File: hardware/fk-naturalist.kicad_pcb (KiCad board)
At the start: 2 copper layers, 28.7 x 87.4 mm, 90 parts, among them J1 MICRO-USB, J2 CONN_01X03, J3 Conn_01x08, J4 Conn_01x02, J5 Conn_01x01, J6 CONN-HDR-2x5, J8 Conn_01x01, M1 MOUNT_HOLE, M2 MOUNT_HOLE, M3 MOUNT_HOLE, M4 MOUNT_HOLE, Q1 2N7002LT1G, Q2 2N7002LT1G, Q3 2N7002LT1G, Q4 2N7002LT1G, SW1 SPNO, U1 ATSAMD21G18A-AU, U101 TSL2591, U102 MPL3115A2, U103 BNO055, U104 SHT31, U2 MCP1700T-XXX2E, U3 MAX4466, U4 S25FL1xxK0XM, Y1 FC-135, Y101 FC-135

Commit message: Just tweaking the locations of things.
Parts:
- moved J5 6.21 mm to (142.8, 120.3), turned to 270 degrees
- moved R27 4.64 mm to (140.9, 123.5), turned to 270 degrees
- moved J8 4.21 mm to (140.6, 120.3), turned to 270 degrees
- moved R26 4.17 mm to (142.6, 123.5), turned to 270 degrees
- moved R6 2.44 mm to (142.4, 130.6)
- moved R29 1.63 mm to (145.7, 130.6)
- moved R28 1.58 mm to (147.3, 130.6)
- moved R7 1.42 mm to (144.0, 130.6)
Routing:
- net /SDA: track 68.9 -> 77.1 mm, vias 4 -> 5
- net /SDA2: track 25.4 -> 17.4 mm
- net /SCL: track 75.0 -> 79.1 mm, vias 3 -> 4
- net /SDA3: track 62.2 -> 59.2 mm
- net /D13: track 36.0 -> 33.4 mm, vias 3 -> 2
- net VUSB: track 35.2 -> 33.4 mm
- net 3V3: track 273.7 -> 272.0 mm
- net /SCL3: track 61.4 -> 62.5 mm

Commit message: Adding D30 and D31 to header.
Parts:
- J3: value Conn_01x08 -> Conn_01x10; footprint Socket_Strips:Socket_Strip_Straight_1x08_Pitch2.54mm -> Socket_Strips:Socket_Strip_Straight_1x10_Pitch2.54mm
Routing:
- net /D30: track 0.00 -> 33.4 mm, vias 0 -> 1
- net /D31: track 0.00 -> 32.7 mm, vias 0 -> 1
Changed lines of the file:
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@@
 (kicad_pcb (version 4) (host pcbnew 4.0.7-e2-6376~58~ubuntu16.04.1)
   (general
-    (links 203)
+    (links 205)
     (no_connects 0)
-    (area 106.352905 47.75 165.914286 159.377948)
+    (area 125.718499 67.742999 154.578121 155.274081)
     (thickness 1.6)
     (drawings 33)
-    (tracks 818)
+    (tracks 840)
     (zones 0)
     (modules 90)
@@
     )
   )
-  (module Socket_Strips:Socket_Strip_Straight_1x08_Pitch2.54mm (layer F.Cu)
+  (module Socket_Strips:Socket_Strip_Straight_1x10_Pitch2.54mm (layer F.Cu)
     (at 152.6286 150.7998 180)
-    (descr "Through hole straight socket strip, 1x08, 2.54mm pitch, single row")
-    (tags "Through hole socket strip THT 1x08 2.54mm single row")
-    (fp_text reference J3 (at 0 -2.33 180) (layer F.SilkS) hide
+    (descr "Through hole straight socket strip, 1x10, 2.54mm pitch, single row")
+    (tags "Through hole socket strip THT 1x10 2.54mm single row")
+    (fp_text reference J3 (at 0 -2.33 180) (layer F.SilkS)
       (effects (font (size 1 1) (thickness 0.15)))
     )
-    (fp_text value Conn_01x08 (at 0 20.11 180) (layer F.Fab) hide
+    (fp_text value Conn_01x10 (at 0 25.19 180) (layer F.Fab)
       (effects (font (size 1 1) (thickness 0.15)))
     )
-    (fp_line (start -1.27 -1.27) (end -1.27 19.05) (layer F.Fab) (width 0.1))
-    (fp_line (start -1.27 19.05) (end 1.27 19.05) (layer F.Fab) (width 0.1))
-    (fp_line (start 1.27 19.05) (end 1.27 -1.27) (layer F.Fab) (width 0.1))
+    (fp_line (start -1.27 -1.27) (end -1.27 24.13) (layer F.Fab) (width 0.1))
+    (fp_line (start -1.27 24.13) (end 1.27 24.13) (layer F.Fab) (width 0.1))
+    (fp_line (start 1.27 24.13) (end 1.27 -1.27) (layer F.Fab) (width 0.1))
     (fp_line (start 1.27 -1.27) (end -1.27 -1.27) (layer F.Fab) (width 0.1))
-    (fp_line (start -1.33 1.27) (end -1.33 19.11) (layer F.SilkS) (width 0.12))
-    (fp_line (start -1.33 19.11) (end 1.33 19.11) (layer F.SilkS) (width 0.12))
-    (fp_line (start 1.33 19.11) (end 1.33 1.27) (layer F.SilkS) (width 0.12))
+    (fp_line (start -1.33 1.27) (end -1.33 24.19) (layer F.SilkS) (width 0.12))
+    (fp_line (start -1.33 24.19) (end 1.33 24.19) (layer F.SilkS) (width 0.12))
+    (fp_line (start 1.33 24.19) (end 1.33 1.27) (layer F.SilkS) (width 0.12))
     (fp_line (start 1.33 1.27) (end -1.33 1.27) (layer F.SilkS) (width 0.12))
     (fp_line (start -1.33 0) (end -1.33 -1.33) (layer F.SilkS) (width 0.12))
     (fp_line (start -1.33 -1.33) (end 0 -1.33) (layer F.SilkS) (width 0.12))
-    (fp_line (start -1.8 -1.8) (end -1.8 19.55) (layer F.CrtYd) (width 0.05))
-    (fp_line (start -1.8 19.55) (end 1.8 19.55) (layer F.CrtYd) (width 0.05))
-    (fp_line (start 1.8 19.55) (end 1.8 -1.8) (layer F.CrtYd) (width 0.05))
+    (fp_line (start -1.8 -1.8) (end -1.8 24.65) (layer F.CrtYd) (width 0.05))
+    (fp_line (start -1.8 24.65) (end 1.8 24.65) (layer F.CrtYd) (width 0.05))
+    (fp_line (start 1.8 24.65) (end 1.8 -1.8) (layer F.CrtYd) (width 0.05))
     (fp_line (start 1.8 -1.8) (end -1.8 -1.8) (layer F.CrtYd) (width 0.05))
-    (fp_text user %R (at 0 -2.33 180) (layer F.Fab) hide
+    (fp_text user %R (at 0 -2.33 180) (layer F.Fab)
       (effects (font (size 1 1) (thickness 0.15)))
     )
@@
     (pad 8 thru_hole oval (at 0 17.78 180) (size 1.7 1.7) (drill 1) (layers *.Cu *.Mask)
       (net 1 GND))
-    (model ${KISYS3DMOD}/Socket_Strips.3dshapes/Socket_Strip_Straight_1x08_Pitch2.54mm.wrl
-      (at (xyz 0 -0.35 0))
+    (pad 9 thru_hole oval (at 0 20.32 180) (size 1.7 1.7) (drill 1) (layers *.Cu *.Mask)
+      (net 43 /D30))
+    (pad 10 thru_hole oval (at 0 22.86 180) (size 1.7 1.7) (drill 1) (layers *.Cu *.Mask)
+      (net 44 /D31))
+    (model ${KISYS3DMOD}/Socket_Strips.3dshapes/Socket_Strip_Straight_1x10_Pitch2.54mm.wrl
+      (at (xyz 0 -0.45 0))
       (scale (xyz 1 1 1))
       (rotate (xyz 0 0 270))
@@
   (segment (start 145.084187 109.081314) (end 145.084187 110.371093) (width 0.254) (layer F.Cu) (net 42))
   (via (at 145.084187 110.371093) (size 0.5) (drill 0.3) (layers F.Cu B.Cu) (net 42))
+  (segment (start 153.010393 114.065693) (end 146.1008 107.1561) (width 0.254) (layer B.Cu) (net 43))
+  (segment (start 145.94839 103.93679) (end 145.94839 107.00369) (width 0.254) (layer B.Cu) (net 43))
+  (segment (start 145.94839 107.00369) (end 146.1008 107.1561) (width 0.254) (layer B.Cu) (net 43))
+  (segment (start 145.5928 103.5812) (end 145.94839 103.93679) (width 0.254) (layer B.Cu) (net 43))
+  (segment (start 144.720458 105.040629) (end 145.5928 104.168287) (width 0.254) (layer F.Cu) (net 43))
+  (segment (start 145.5928 104.168287) (end 145.5928 103.5812) (width 0.254) (layer F.Cu) (net 43))
+  (via (at 145.5928 103.5812) (size 0.5) (drill 0.3) (layers F.Cu B.Cu) (net 43))
+  (segment (start 153.010393 115.789712) (end 153.010393 114.065693) (width 0.254) (layer B.Cu) (net 43))
+  (segment (start 150.82525 128.67645) (end 150.82525 127.3207) (width 0.254) (layer B.Cu) (net 43))
+  (segment (start 150.82525 127.3207) (end 153.010394 125.135556) (width 0.254) (layer B.Cu) (net 43))
+  (segment (start 153.010394 125.135556) (end 153.010393 115.789712) (width 0.254) (layer B.Cu) (net 43))
+  (segment (start 152.6286 130.4798) (end 150.82525 128.67645) (width 0.254) (layer B.Cu) (net 43))
+  (segment (start 146.3548 102.108) (end 146.104801 102.357999) (width 0.254) (layer F.Cu) (net 44))
+  (segment (start 145.856518 102.357999) (end 144.897234 103.317283) (width 0.254) (layer F.Cu) (net 44))
+  (segment (start 146.104801 102.357999) (end 145.856518 102.357999) (width 0.254) (layer F.Cu) (net 44))
+  (segment (start 144.897234 103.317283) (end 144.897234 104.156747) (width 0.254) (layer F.Cu) (net 44))
+  (segment (start 144.897234 104.156747) (end 144.366905 104.687076) (width 0.254) (layer F.Cu) (net 44))
+  (segment (start 146.3548 102.108) (end 146.3548 106.7308) (width 0.254) (layer B.Cu) (net 44))
+  (segment (start 153.478599 127.089801) (end 152.6286 127.9398) (width 0.254) (layer B.Cu) (net 44))
+  (segment (start 146.3548 106.7308) (end 153.478599 113.854599) (width 0.254) (layer B.Cu) (net 44))
+  (segment (start 153.478599 113.854599) (end 153.478599 127.089801) (width 0.254) (layer B.Cu) (net 44))
+  (via (at 146.3548 102.108) (size 0.5) (drill 0.3) (layers F.Cu B.Cu) (net 44))
   (segment (start 143.7005 106.045) (end 144.8816 106.045) (width 0.254) (layer F.Cu) (net 46))
   (segment (start 146.1008 103.7862) (end 146.1008 104.8258) (width 0.254) (layer F.Cu) (net 46))
@@
     (connect_pads (clearance 0.2032))
     (min_thickness 0.253)
-    (fill (arc_segments 32) (thermal_gap 0.254) (thermal_bridge_width 0.254) (smoothing chamfer))
+    (fill yes (arc_segments 32) (thermal_gap 0.254) (thermal_bridge_width 0.254) (smoothing chamfer))
     (polygon
       (pts
@@
     (connect_pads (clearance 0.2032))
     (min_thickness 0.253)
-    (fill (arc_segments 32) (thermal_gap 0.254) (thermal_bridge_width 0.254) (smoothing chamfer))
+    (fill yes (arc_segments 32) (thermal_gap 0.254) (thermal_bridge_width 0.254) (smoothing chamfer))
     (polygon
       (pts
@@
     (connect_pads (clearance 0.2032))
     (min_thickness 0.253)
-    (fill (arc_segments 32) (thermal_gap 0.254) (thermal_bridge_width 0.254) (smoothing chamfer))
+    (fill yes (arc_segments 32) (thermal_gap 0.254) (thermal_bridge_width 0.254) (smoothing chamfer))
     (polygon
       (pts
@@
     (connect_pads (clearance 0.2032))
     (min_thickness 0.253)
-    (fill (arc_segments 32) (thermal_gap 0.254) (thermal_bridge_width 0.254) (smoothing chamfer))
+    (fill yes (arc_segments 32) (thermal_gap 0.254) (thermal_bridge_width 0.254) (smoothing chamfer))
     (polygon
       (pts

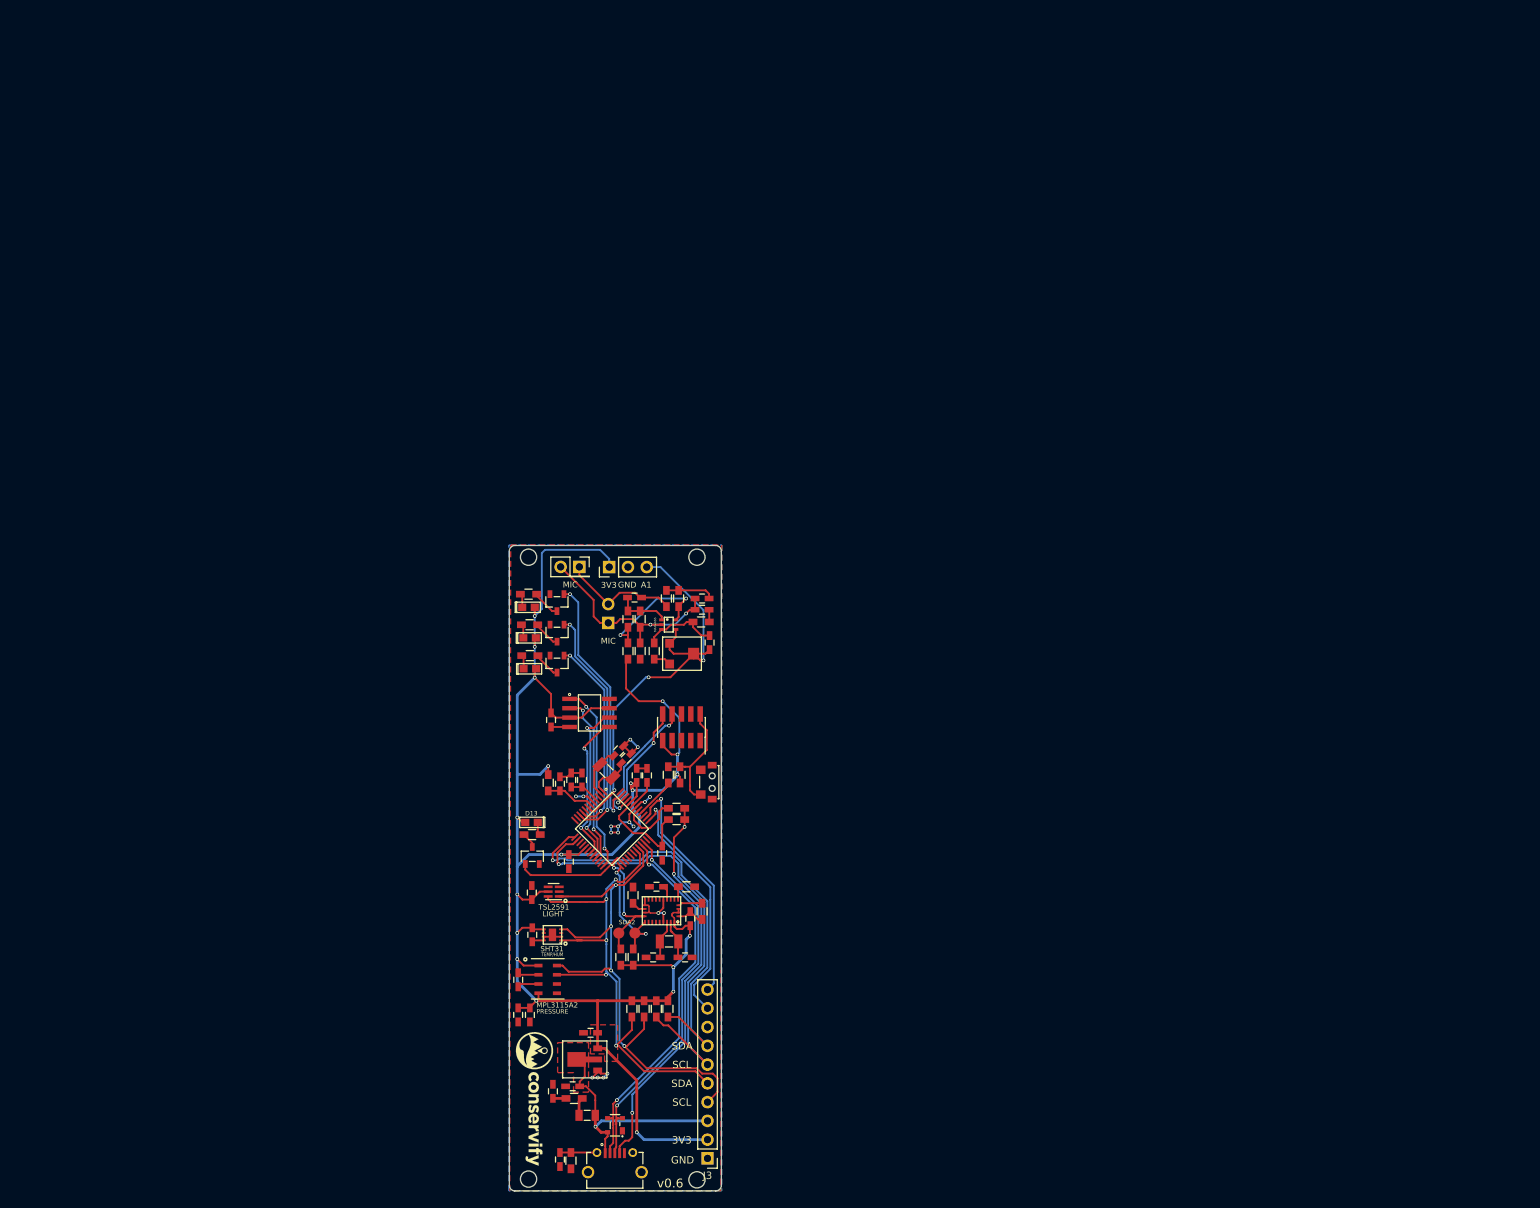
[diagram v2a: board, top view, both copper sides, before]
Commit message: Starting on the combined coreless board. Schematic is... done hopefully.
This includes the change to the new I2S chip.
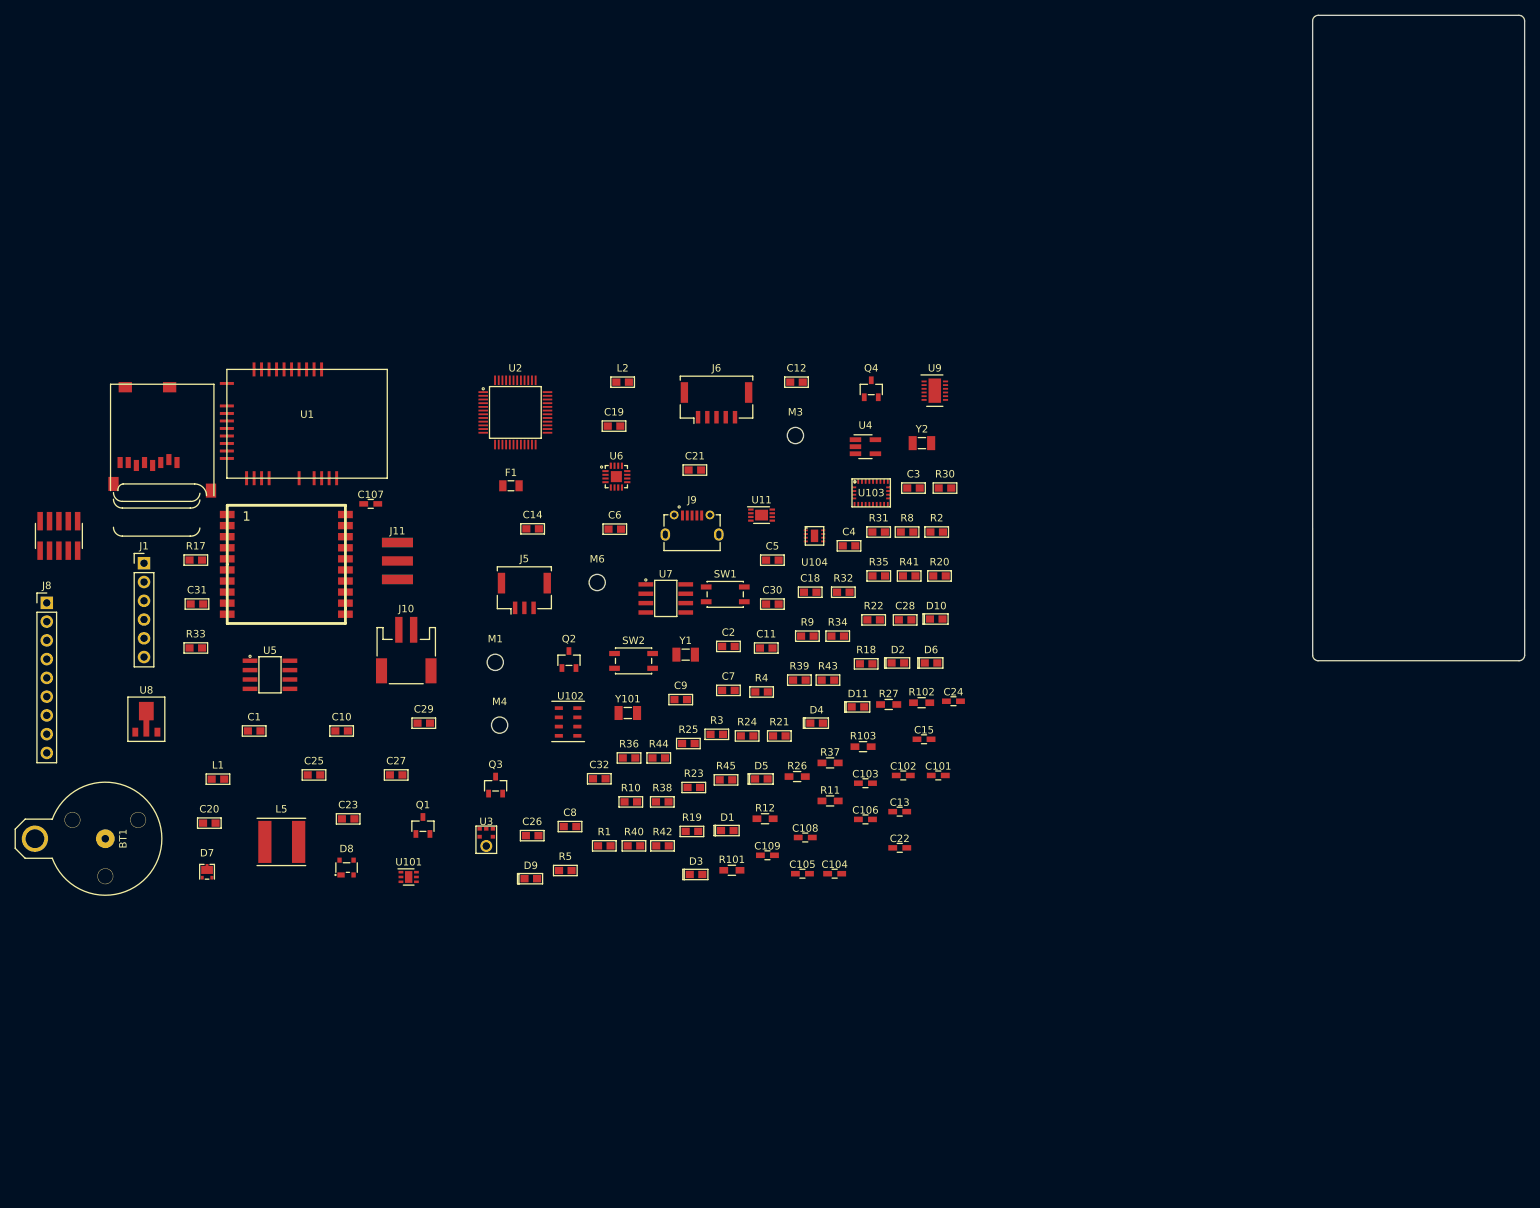
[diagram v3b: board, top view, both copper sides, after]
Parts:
- removed C16: 10uF, Capacitors_SMD:C_0603_HandSoldering
- removed C17: 100pF, Capacitors_SMD:C_0603_HandSoldering
- removed G***: LOGO, conservify:conservify_text_negative_4000
- removed J2: CONN_01X03, Socket_Strips:Socket_Strip_Straight_1x03_Pitch2.54mm
- removed J3: Conn_01x10, Socket_Strips:Socket_Strip_Straight_1x10_Pitch2.54mm
- removed J4: Conn_01x02, Socket_Strips:Socket_Strip_Straight_2x01_Pitch2.54mm
- removed L3, L4: WE-CBF, Resistors_SMD:R_0603_HandSoldering
- removed M2: MOUNT_HOLE, RocketScreamKicadLibrary:HOLE_NPTH_2.2MM
- removed MK1: CMA-4544PF-W, Socket_Strips:Socket_Strip_Straight_1x02_Pitch2.54mm
- removed R13: 1k, Resistors_SMD:R_0603_HandSoldering
- removed R14, R15: 1M, Resistors_SMD:R_0603_HandSoldering
- removed R16: 22k, Resistors_SMD:R_0603_HandSoldering
- removed R28, R29, R6, R7: 4.7K, Resistors_SMD:R_0603_HandSoldering
- removed RV1: TC33X-2-104E (100K), conservify:BOURNS-TC33X-2
- added BT1: Battery_Cell, Connectors:CR1220, F.Cu at (61.6, 107.5)
- added C19: 4.7uF 10V X5R, RocketScreamKicadLibrary:CAP-0603, F.Cu at (140.0, 51.7)
- added C20: 4.7uF 10V X5R, RocketScreamKicadLibrary:CAP-0603, F.Cu at (85.2, 105.4)
- added C21: 1uF 10V X5R, RocketScreamKicadLibrary:CAP-0603, F.Cu at (150.9, 57.6)
- added C22: 10uF, Capacitors_SMD:C_0603_HandSoldering, F.Cu at (178.7, 108.8)
- added C23: 1uF 10V X5R, RocketScreamKicadLibrary:CAP-0603, F.Cu at (104.0, 104.8)
- added C24: 10uF, Capacitors_SMD:C_0603_HandSoldering, F.Cu at (185.9, 88.9)
- added C25: 4.7uF 10V X5R, RocketScreamKicadLibrary:CAP-0603, F.Cu at (99.3, 98.9)
- added C26: 100nF, RocketScreamKicadLibrary:CAP-0603, F.Cu at (128.9, 107.1)
- added C27: 1uF 10V X5R, RocketScreamKicadLibrary:CAP-0603, F.Cu at (110.5, 98.9)
- added C28: 10nF, RocketScreamKicadLibrary:CAP-0603, F.Cu at (179.4, 77.9)
- added C29: 1uF 10V X5R, RocketScreamKicadLibrary:CAP-0603, F.Cu at (114.2, 91.9)
- added C30: 100pF, RocketScreamKicadLibrary:CAP-0603, F.Cu at (161.4, 75.8)
- added C31: 10uF, RocketScreamKicadLibrary:CAP-0603, F.Cu at (83.5, 75.7)
- added C32: 10uF, RocketScreamKicadLibrary:CAP-0603, F.Cu at (138.0, 99.4)
- added D10: Red, RocketScreamKicadLibrary:LED-0603, F.Cu at (183.6, 77.8)
- added D11: Red, RocketScreamKicadLibrary:LED-0603, F.Cu at (173.0, 89.7)
- added D6: Blue, RocketScreamKicadLibrary:LED-0603, F.Cu at (182.9, 83.7)
- added D7: PMEG3020CPA, RocketScreamKicadLibrary:SOT-1016, F.Cu at (84.9, 112.0)
- added D8: PRTR5V0U2X, RocketScreamKicadLibrary:SOT-143B, F.Cu at (103.8, 111.4)
- added D9: Green, RocketScreamKicadLibrary:LED-0603, F.Cu at (128.7, 112.9)
- added J10: S2B-PH-SM4-TB, RocketScreamKicadLibrary:S2B-PH-SM4-TB, F.Cu at (111.8, 82.0)
- added J11: RF-SMA-EDGE, RocketScreamKicadLibrary:RF-SMA-EDGE, F.Cu at (110.7, 69.9)
- added J7: CONN-HDR-2x5, conservify:HDR_2x5_Pitch1.27mm_SMD_JTAG_SWD, F.Cu at (64.8, 66.5)
- added J9: MICRO-USB, RocketScreamKicadLibrary:MICRO-USB, F.Cu at (150.5, 65.2)
- added L5: 22uH, conservify:WURTH_L_6.0x6.0, F.Cu at (94.9, 108.0)
- added M6: MOUNT_HOLE, RocketScreamKicadLibrary:HOLE_NPTH_2.2MM, F.Cu at (137.7, 72.8)
- added M7: MICROSD, conservify:MICROSD, F.Cu at (71.8, 45.9)
- added R18: 2K2, RocketScreamKicadLibrary:RES-0603, F.Cu at (174.1, 83.8)
- added R19: 2K2, RocketScreamKicadLibrary:RES-0603, F.Cu at (150.5, 106.5)
- added R20: 2K2, RocketScreamKicadLibrary:RES-0603, F.Cu at (184.0, 71.9)
- added R21: 1K18, RocketScreamKicadLibrary:RES-0603, F.Cu at (162.4, 93.6)
- added R22: 46K4, RocketScreamKicadLibrary:RES-0603, F.Cu at (175.1, 77.9)
- added R23: 100K, RocketScreamKicadLibrary:RES-0603, F.Cu at (150.8, 100.6)
- added R24: 2K94, RocketScreamKicadLibrary:RES-0603, F.Cu at (158.0, 93.6)
- added R25: 2K2, RocketScreamKicadLibrary:RES-0603, F.Cu at (150.0, 94.6)
- added R30: 330R, RocketScreamKicadLibrary:RES-0603, F.Cu at (184.8, 60.0)
- added R31: 1M, RocketScreamKicadLibrary:RES-0603, F.Cu at (175.8, 66.0)
- added R32: 10K, RocketScreamKicadLibrary:RES-0603, F.Cu at (171.0, 74.1)
- added R33: 2K2, RocketScreamKicadLibrary:RES-0603, F.Cu at (83.3, 81.7)
- added R34: 10K, RocketScreamKicadLibrary:RES-0603, F.Cu at (170.3, 80.1)
- added R35: 4.7K, RocketScreamKicadLibrary:RES-0603, F.Cu at (175.8, 71.9)
- added R36: 4.7K, RocketScreamKicadLibrary:RES-0603, F.Cu at (142.0, 96.6)
- added R37: 1k, Resistors_SMD:R_0603_HandSoldering, F.Cu at (169.2, 97.3)
- added R38: 100k, RocketScreamKicadLibrary:RES-0603, F.Cu at (146.5, 102.5)
- added R39: 1k, RocketScreamKicadLibrary:RES-0603, F.Cu at (165.1, 86.0)
- added R40: 1k, RocketScreamKicadLibrary:RES-0603, F.Cu at (142.7, 108.5)
- added R41: 180R, RocketScreamKicadLibrary:RES-0603, F.Cu at (179.9, 71.9)
- added R42: 4.7K, RocketScreamKicadLibrary:RES-0603, F.Cu at (146.5, 108.5)
- added R43: 4.7K, RocketScreamKicadLibrary:RES-0603, F.Cu at (168.9, 86.0)
- added R44: 100k, RocketScreamKicadLibrary:RES-0603, F.Cu at (146.0, 96.6)
- added R45: 22K1, RocketScreamKicadLibrary:RES-0603, F.Cu at (155.1, 99.6)
- added SW2: SPNO, conservify:SW_SPST_WURTH_1, F.Cu at (142.6, 83.4)
- added U10: FGPMMOPA6H, conservify:FGPMMOPA6H, F.Cu at (95.6, 70.4)
- added U11: MAX1704XX, Housings_DFN_QFN:DFN-8-1EP_3x2mm_Pitch0.5mm, F.Cu at (159.9, 63.7)
- added U5: S25FL116K0XMFI041, RocketScreamKicadLibrary:SOIC-8-N, F.Cu at (93.4, 85.3)
- added U6: BQ24074RGTT, RocketScreamKicadLibrary:QFN-16_3x3mm, F.Cu at (140.3, 58.5)
- added U7: PCF8523, RocketScreamKicadLibrary:SOIC-8-N, F.Cu at (147.0, 75.0)
- added U8: MCP1700T-3302E/MB, RocketScreamKicadLibrary:SOT-89, F.Cu at (76.7, 91.3)
- added U9: ISL8541x, Housings_DFN_QFN:DFN-12-1EP_3x4mm_Pitch0.5mm, F.Cu at (183.4, 46.9)
- added Y2: FC-135, RocketScreamKicadLibrary:ABS07, F.Cu at (181.7, 54.0)
- C1: value 18pF -> 4.7uF 10V X5R; footprint Capacitors_SMD:C_0603_HandSoldering -> RocketScreamKicadLibrary:CAP-0603
- C10: value 4.7nF -> 4.7uF 10V X5R; footprint Capacitors_SMD:C_0603_HandSoldering -> RocketScreamKicadLibrary:CAP-0603
- C11: value 1uF -> 100nF; footprint Capacitors_SMD:C_0603_HandSoldering -> RocketScreamKicadLibrary:CAP-0603
- C12: value 1uF -> 1uF 50V X5R; footprint Capacitors_SMD:C_0603_HandSoldering -> RocketScreamKicadLibrary:CAP-0603
- C13: value 0.1uF -> 1uF
- C14: value 4.7uF 10V X5R -> 4.7nF 25V X7R; footprint Capacitors_SMD:C_0603_HandSoldering -> RocketScreamKicadLibrary:CAP-0603
- C15: value 0.01uF -> 220pF
- C18, C7, C8: footprint Capacitors_SMD:C_0603_HandSoldering -> RocketScreamKicadLibrary:CAP-0603
- C2: value 18pF -> 100nF; footprint Capacitors_SMD:C_0603_HandSoldering -> RocketScreamKicadLibrary:CAP-0603
- C3, C4: value 100nF -> 18pF; footprint Capacitors_SMD:C_0603_HandSoldering -> RocketScreamKicadLibrary:CAP-0603
- C5: value 1uF 10V X5R -> 100nF; footprint Capacitors_SMD:C_0603_HandSoldering -> RocketScreamKicadLibrary:CAP-0603
- C6: value 100nF -> 1uF 10V X5R; footprint Capacitors_SMD:C_0603_HandSoldering -> RocketScreamKicadLibrary:CAP-0603
- C9: value 4.7uF -> 100nF; footprint Capacitors_SMD:C_0603_HandSoldering -> RocketScreamKicadLibrary:CAP-0603
- D2: value Yellow -> Green
- D3: value Blue -> Yellow
- D4: value PRTR5V0U2X -> Orange; footprint RocketScreamKicadLibrary:SOT-143B -> RocketScreamKicadLibrary:LED-0603
- D5: value Orange -> Yellow
- J1: value MICRO-USB -> CONN_01X06; footprint conservify:MICRO-USB -> Socket_Strips:Socket_Strip_Straight_1x06_Pitch2.54mm
- J5: value Conn_01x01 -> Conn_01x03; footprint Measurement_Points:Measurement_Point_Round-SMD-Pad_Small -> conservify:Molex_CLIK-Mate_502382-0370_1x03_P1.25mm_Vertical
- J6: value CONN-HDR-2x5 -> Conn_01x05; footprint Socket_Strips:Socket_Strip_Straight_2x05_Pitch1.27mm_SMD -> conservify:Molex_CLIK-Mate_502382-0570_1x05_P1.25mm_Vertical
- J8: value Conn_01x01 -> Conn_01x09; footprint Measurement_Points:Measurement_Point_Round-SMD-Pad_Small -> Socket_Strips:Socket_Strip_Straight_1x09_Pitch2.54mm
- L1, L2: footprint Inductors_SMD:L_0603_HandSoldering -> RocketScreamKicadLibrary:IND-0603
- R1: value 2k2 -> 100k; footprint Resistors_SMD:R_0603_HandSoldering -> RocketScreamKicadLibrary:RES-0603
- R10: value 1M -> 330R; footprint Resistors_SMD:R_0603_HandSoldering -> RocketScreamKicadLibrary:RES-0603
- R11: value 1k -> 10K
- R12: value 1k -> 68R
- R17: value 2k2 -> 10K; footprint Resistors_SMD:R_0603_HandSoldering -> RocketScreamKicadLibrary:RES-0603
- R2: value 330R -> 100k; footprint Resistors_SMD:R_0603_HandSoldering -> RocketScreamKicadLibrary:RES-0603
- R3: value 2k2 -> 2K2; footprint Resistors_SMD:R_0603_HandSoldering -> RocketScreamKicadLibrary:RES-0603
- R4: value 10K -> 1k; footprint Resistors_SMD:R_0603_HandSoldering -> RocketScreamKicadLibrary:RES-0603
- R5: value 2k2 -> 1k; footprint Resistors_SMD:R_0603_HandSoldering -> RocketScreamKicadLibrary:RES-0603
- R8: value 100k -> 10K; footprint Resistors_SMD:R_0603_HandSoldering -> RocketScreamKicadLibrary:RES-0603
- R9: footprint Resistors_SMD:R_0603_HandSoldering -> RocketScreamKicadLibrary:RES-0603
- SW1: footprint RocketScreamKicadLibrary:TS-018 -> conservify:SW_SPST_WURTH_1
- U1: value ATSAMD21G18A-AU -> ATWINC1500-MR210PA; footprint RocketScreamKicadLibrary:TQFP-48_7x7mm_Pitch0.5mm -> conservify:ATMEL_ATWINC1500-MR210PA
- U2: value MCP1700T-XXX2E -> ATSAMD21G18A-AU; footprint RocketScreamKicadLibrary:SOT-89 -> RocketScreamKicadLibrary:TQFP-48_7x7mm_Pitch0.5mm
- U3: value MAX4466 -> SPH0645; footprint conservify:SC70-5 -> conservify:SPH0645LM4H-B
- U4: value S25FL1xxK0XM -> 24AA02E64; footprint RocketScreamKicadLibrary:SOIC-8-N -> TO_SOT_Packages_SMD:SOT-23-5_HandSoldering
- moved J1 103.3 mm to (76.3, 70.2)
- moved C12 92.4 mm to (164.7, 45.7), turned to 0 degrees
- moved J8 89.4 mm to (63.2, 75.6), turned to 0 degrees
- moved U2 88.1 mm to (126.6, 49.8), turned to 0 degrees
- moved F1 85.9 mm to (126.0, 59.7)
- moved Q4 78.1 mm to (174.8, 46.6)
- moved C107 72.3 mm to (107.0, 62.2), turned to 0 degrees
- moved M1 70.1 mm to (123.9, 83.6)
- moved U1 68.6 mm to (98.4, 51.3), turned to 0 degrees
- moved C10 65.1 mm to (103.1, 92.9), turned to 0 degrees
- moved C11 64.9 mm to (160.6, 81.7), turned to 0 degrees
- moved L1 64.8 mm to (86.3, 99.5)
- moved U104 64.6 mm to (167.1, 66.5), turned to 0 degrees
- moved U103 63.3 mm to (174.8, 60.7), turned to 0 degrees
- moved D4 60.9 mm to (167.4, 91.9), turned to 0 degrees
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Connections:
- net /A0 renamed Net-(U1-Pad3)
- C1 pad 1: GND -> AREF
- C1 pad 2: Net-(C1-Pad2) -> GND
- C10 pad 1: Net-(C10-Pad1) -> 5V0
- C11 pad 1: VUSB -> 3V3
- C12 pad 1: 3V3 -> GND
- C12 pad 2: GND -> VEXT
- C13 pad 1: Net-(C13-Pad1) -> 3V3
- C13 pad 2: /AGND -> GND
- C14 pad 1: AREF -> Net-(C14-Pad1)
- C15 pad 1: Net-(C15-Pad1) -> 3V3
- C15 pad 2: Net-(C15-Pad2) -> GND
- C2 pad 1: GND -> AREF
- C2 pad 2: Net-(C2-Pad2) -> GND
- C3 pad 1: 3V3 -> GND
- C3 pad 2: GND -> Net-(C3-Pad2)
- C4 pad 1: Net-(C4-Pad1) -> GND
- C4 pad 2: GND -> Net-(C4-Pad2)
- C5 pad 1: Net-(C5-Pad1) -> 3V3
- C6 pad 1: AREF -> Net-(C6-Pad1)
- C7 pad 1: 3V3 -> Net-(C7-Pad1)
- C9 pad 1: 5V0 -> 3V3
- D4 pad 1: GND -> Net-(D4-Pad1)
- D4 pad 2: /USB+ -> 3V3
- J1 pad 1: VUSB -> VBAT
- J1 pad 2: /USB- -> GND
- J1 pad 3: /USB+ -> VIN
- J1 pad 4: Net-(J1-Pad4) -> 5V0
- J1 pad 5: GND -> VBUS
- J1 pad 6: Net-(C10-Pad1) -> 3V3
- J5 pad 1: /SDA2 -> GND
- J6 pad 1: GND -> 3V3
- J6 pad 2: /RST -> GND
- J6 pad 3: Net-(J6-Pad3) -> GND
- J6 pad 4: Net-(J6-Pad4) -> /SCL
- J6 pad 5: GND -> /SDA
- J8 pad 1: /D13 -> /RADIO_RST
- L1 pad 1: 5V0 -> Net-(C7-Pad1)
- L1 pad 2: Net-(F1-Pad1) -> 3V3
- L2 pad 1: Net-(C4-Pad1) -> 5V0
- L2 pad 2: 3V3 -> Net-(F1-Pad1)
- Q1 pad 1: /A3 -> /D13
- Q2 pad 1: /A4 -> /A3
- Q3 pad 1: /A5 -> /A4
- Q4 pad 1: /D13 -> /A5
- R1 pad 1: Net-(D1-Pad1) -> /WIFI_RST
- R1 pad 2: Net-(Q1-Pad3) -> GND
- R10 pad 1: Net-(C10-Pad1) -> /USER_SW
- R10 pad 2: GND -> Net-(R10-Pad2)
- R11 pad 1: /AVCC -> GND
- R11 pad 2: Net-(C13-Pad1) -> Net-(R11-Pad2)
- R12 pad 1: Net-(C13-Pad1) -> Net-(R12-Pad1)
- R12 pad 2: Net-(C15-Pad2) -> /I2S_DATA
- R17 pad 1: Net-(D5-Pad1) -> 3V3
- R17 pad 2: Net-(Q4-Pad3) -> Net-(R10-Pad2)
- R2 pad 1: /RESET -> /WIFI_EN
- R2 pad 2: /RST -> GND
- R27 pad 1: /D13 -> /SCL2
- R3 pad 1: Net-(D2-Pad1) -> Net-(D1-Pad1)
- R3 pad 2: Net-(Q2-Pad3) -> Net-(Q1-Pad3)
- R4 pad 1: 3V3 -> Net-(R4-Pad1)
- R4 pad 2: /RST -> Net-(D2-Pad1)
- R5 pad 1: Net-(D3-Pad1) -> Net-(R5-Pad1)
- R5 pad 2: Net-(Q3-Pad3) -> Net-(D3-Pad1)
- R8 pad 2: Net-(J1-Pad4) -> /RST
- R9 pad 1: Net-(J1-Pad4) -> /RESET
- R9 pad 2: /USB_ID -> /RST
- U1 pad 1: Net-(C2-Pad2) -> Net-(U1-Pad1)
- U1 pad 10: /A4 -> 3V3
- U1 pad 11: /D8 -> /WIFI_WAKE
- U1 pad 12: /D9 -> GND
- U1 pad 13: /SDA3 -> /WIFI_IRQ
- U1 pad 14: /SCL3 -> Net-(U1-Pad14)
- U1 pad 15: /D1 -> /MOSI
- U1 pad 16: /D0 -> /WIFI_CS
- U1 pad 17: 3V3 -> /MISO
- U1 pad 18: GND -> /SCK
- U1 pad 19: /MOSI -> Net-(U1-Pad19)
- U1 pad 2: Net-(C1-Pad2) -> Net-(U1-Pad2)
- U1 pad 20: /SCK -> 3V3
- U1 pad 21: /MISO -> Net-(U1-Pad21)
- U1 pad 22: /ATN -> /WIFI_EN
- U1 pad 23: /D2 -> 3V3
- U1 pad 24: /D5 -> Net-(U1-Pad24)
- U1 pad 25: /SDA2 -> (no net)
- U1 pad 26: /D13 -> Net-(R4-Pad1)
- U1 pad 27: /D10 -> Net-(R5-Pad1)
- U1 pad 28: /D12 -> GND
- U1 pad 4: AREF -> /WIFI_RST
- U1 pad 5: GND -> (no net)
- U1 pad 6: Net-(C4-Pad1) -> (no net)
- U1 pad 7: /A1 -> (no net)
- U1 pad 8: /A2 -> (no net)
- U1 pad 9: /A3 -> GND
- U103 pad 19: /D13 -> /SCL2
- U2 pad 1: GND -> Net-(C4-Pad2)
- U2 pad 2: VUSB -> Net-(C3-Pad2)
- U2 pad 3: 3V3 -> Net-(U2-Pad3)
- U3 pad 1: Net-(C15-Pad1) -> /I2S_WS
- U3 pad 2: /AGND -> Net-(R11-Pad2)
- U3 pad 3: Net-(C17-Pad2) -> GND
- U3 pad 4: /A1 -> /I2S_BCLK
- U3 pad 5: /AVCC -> 3V3
- U4 pad 1: /D5 -> /SCL
- U4 pad 2: /MISO -> GND
- U4 pad 3: 3V3 -> /SDA
- U4 pad 4: GND -> 3V3
- U4 pad 5: /MOSI -> Net-(U4-Pad5)
- Y1 pad 1: Net-(C1-Pad2) -> Net-(C3-Pad2)
- Y1 pad 2: Net-(C2-Pad2) -> Net-(C4-Pad2)
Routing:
- net 3V3: track 272.0 -> 0.00 mm, vias 19 -> 0
- net /SCL: track 79.1 -> 0.00 mm, vias 4 -> 0
- net /SDA: track 77.1 -> 0.00 mm, vias 5 -> 0
- net /SCL3: track 62.5 -> 0.00 mm, vias 1 -> 0
- net /SDA3: track 59.2 -> 0.00 mm, vias 1 -> 0
- net /A1: track 58.3 -> 0.00 mm, vias 3 -> 0
- net Net-(J1-Pad4): track 53.7 -> 0.00 mm, vias 3 -> 0
- net GND: track 51.8 -> 0.00 mm, vias 18 -> 0
- net /USB-: track 51.4 -> 0.00 mm, vias 2 -> 0
- net /USB+: track 51.3 -> 0.00 mm, vias 2 -> 0
- net /A5: track 35.6 -> 0.00 mm, vias 2 -> 0
- net /D30: track 33.4 -> 0.00 mm, vias 1 -> 0
- net /D13: track 33.4 -> 0.00 mm, vias 2 -> 0
- net VUSB: track 33.4 -> 0.00 mm, vias 1 -> 0
- net /D31: track 32.7 -> 0.00 mm, vias 1 -> 0
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- removed copper zone on F.Cu, net 3V3
- removed copper zone on B.Cu, net GND
- removed copper zone on F.Cu, net GND
- removed copper zone on F.Cu, net VUSB
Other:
- board text removed: "3V3"
- board text removed: "A1"
- board text removed: "D13"
- board text removed: "GND"
- board text removed: "LIGHT"
- board text removed: "MIC"
- board text removed: "MPL3115A2"
- board text removed: "PRESSURE"
- board text removed: "SCL"
- board text removed: "SDA"
- board text removed: "SDA2"
- board text removed: "SHT31"
- board text removed: "TEMP/HUM"
- board text removed: "TSL2591"
- board text removed: "v0.6"
